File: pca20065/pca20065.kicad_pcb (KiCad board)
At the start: 6 copper layers, 53 x 53 mm, 319 parts, among them J1 MM8130-2600, J2 MM8130-2600, J3 HDR-3, 1mm, J4 SF72S006VBxR2500, J6 USB-C 2.0, M1 nRF9151-LACAA1A, P1 HDR-4, 1mm, P8 Pin Header 2x5, P9 Card Edge, 0.8mm, Q1 RV2C010UNT2L, Q13 DMC2990UDJ, Q14 RV2C010UNT2L, Q2 DMN2990UDJ, Q3 RV2C010UNT2L, Q4 DMN2990UDJ, Q5 RV2C010UNT2L, Q6 DMC2990UDJ, SW1 Switch, SW2 AYZ0102AGRLC, SW3 PB SW, SW4 L-KLS7-TS5401A-1.35-250-T, U1 NLAS5223BMNR2G, U10 TCK106AG, U11 nPM1300-QEAAC0, U12 FSA2466UMX, U13 TCK106AG, U14 TCK106AG, U15 MFFx_M2M_UICC, U16 NX3DV2567, U17 QM13345, U18 BMI270, U2 TCK106AG, U20 ADXL367, U21 nRF7002-QFAAB0, U22 BGS12xN6, U23 BME688, U24 TXS0102YZPR, U25 nPM6001-CAAAF0, U26 BMM350, U3 TCK106AG, U4 TCK106AG, U5 TCK108AG, U6 nRF5340-CMAAD0, U7 GD25LE255ELIG, U8 ECMF02-4CMX8, U9 SKY65943-11, X1 32MHz, X2 32.768kHz, X3 40MHz

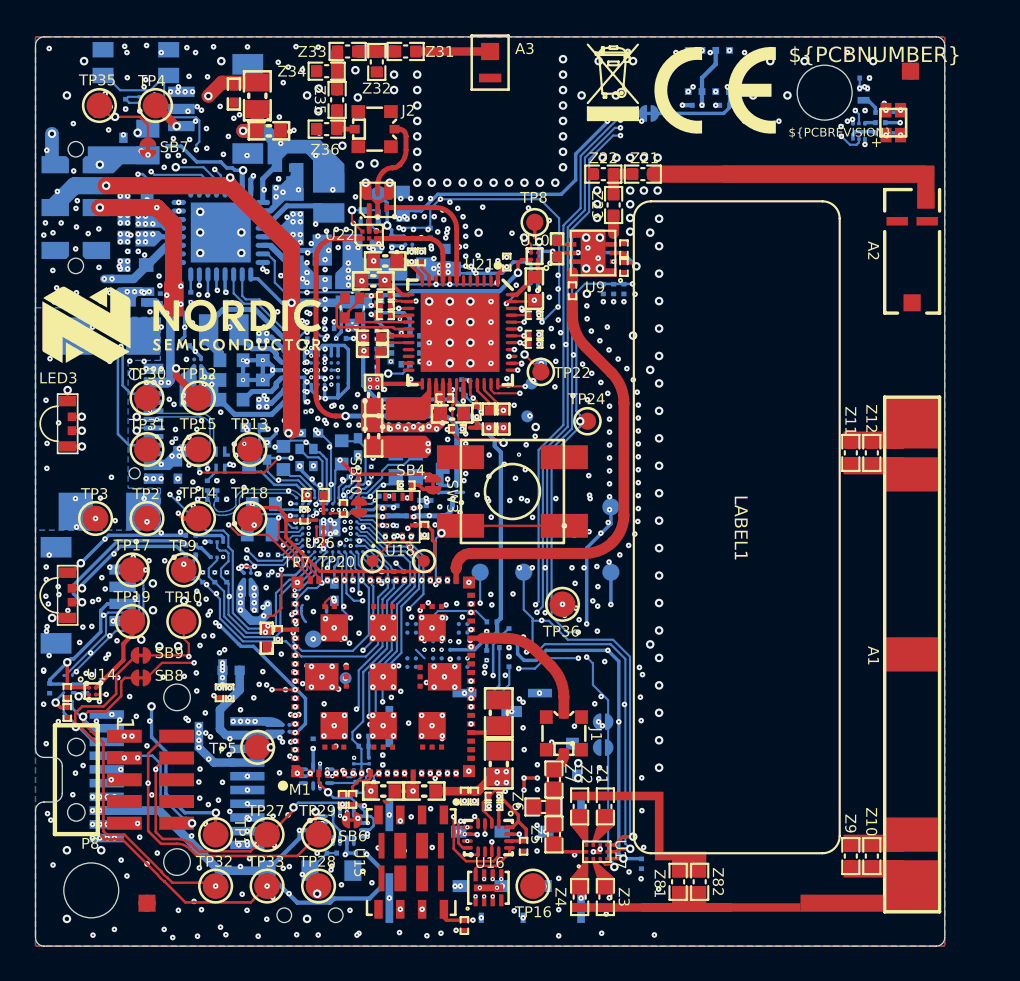
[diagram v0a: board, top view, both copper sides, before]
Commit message: Replaced nrf5340 with nrf54l15
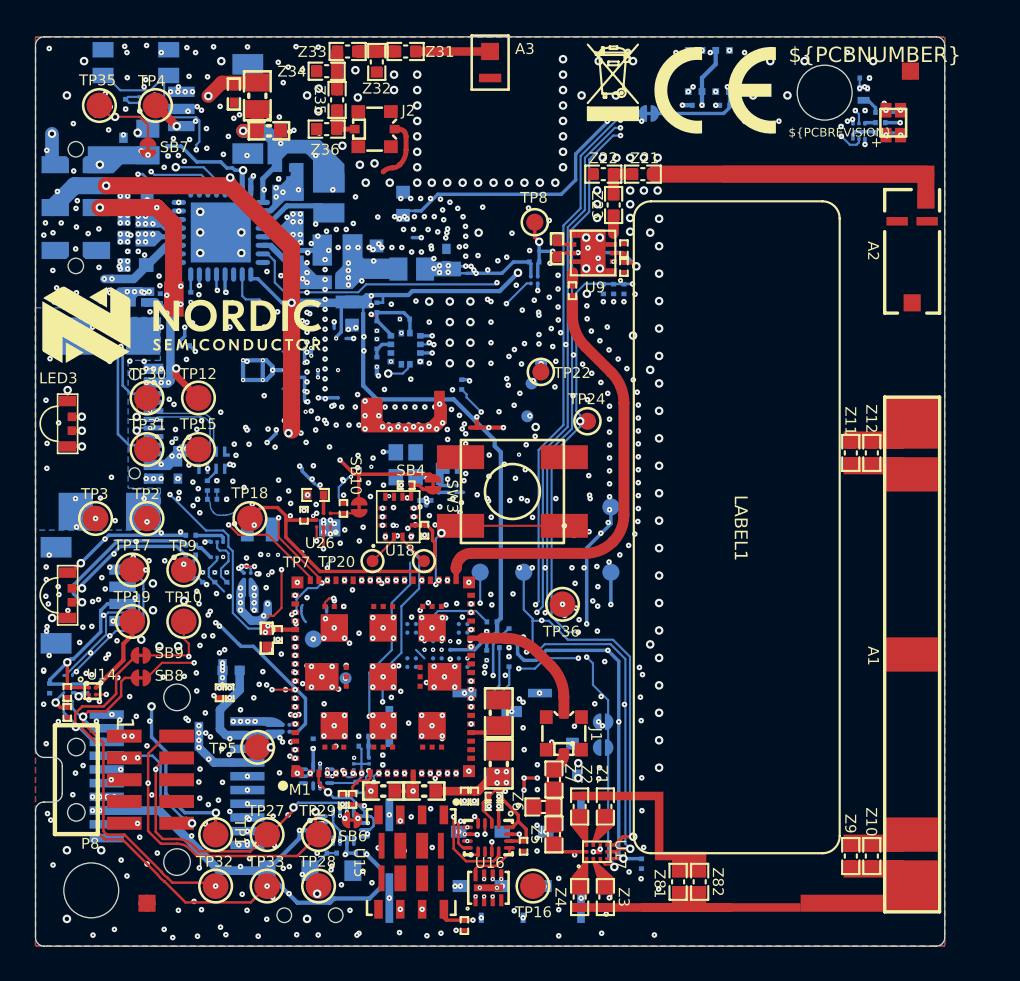
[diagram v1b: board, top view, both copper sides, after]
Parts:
- removed C12, C13, C19, C20, C21, C28, C41, C62: 100nF, pca20065-import-fps:CAPC0603X03L_C
- removed C15, C16, C17, C22, C23, C29, C45, C72, C73: 1.0µF, pca20065-import-fps:CAPC1005X04L
- removed C18: 2.2nF, pca20065-import-fps:CAPC0603X03L_C
- removed C24: 0.7pF, pca20065-import-fps:CAPC0603X03L_C
- removed C25: N.C., pca20065-import-fps:CAPC0603X03L_C_NC
- removed C26, C27, C63, C64, C65, C68, C81: 4.7µF, pca20065-import-fps:CAPC1608X06L
- removed C30, C67: 2.2µF, pca20065-import-fps:CAPC1608X06L
- removed C42: 2.2µF, pca20065-import-fps:CAPC1005X04L
- removed C60, C61: 0.47µF, pca20065-import-fps:CAPC0603X03L_C
- removed C66: 10nF, pca20065-import-fps:CAPC0603X03L_C
- removed C69: 22nF, pca20065-import-fps:CAPC0603X03L_C
- removed C70: 0.22µF, pca20065-import-fps:CAPC0603X03L_C
- removed C71: 2.2µF, pca20065-import-fps:CAPC0603X03L_C
- removed C77, C78, C80: 10µF, pca20065-import-fps:CAPC1608X06L
- removed C82, C83, C84, C85: 1.0µF, pca20065-import-fps:CAPC0603X03L_C
- removed F2: LFD_Diplexer, pca20065-import-fps:CAF-50P160X80-6N
- removed L1, L2: 10µH, pca20065-import-fps:INDC1608X06L
- removed L10: 470nH, pca20065-import-fps:INDC1608X06L
- removed L3, L4: 2.2nH, pca20065-import-fps:INDC0603X03L_C
- removed L6: 3.3µH, pca20065-import-fps:INDC2520X10N
- removed L9: 2.2µH, pca20065-import-fps:INDC2016X10N
- removed Q5: RV2C010UNT2L, pca20065-import-fps:DFN65P100X40-3L
- removed R10: 2R2, pca20065-import-fps:RESC1005X04L
- removed R11: 0R, pca20065-import-fps:RESC0603X03L_C
- removed R16, R4, R6: 150R, pca20065-import-fps:RESC0603X03L_C
- removed R25: N.C., pca20065-import-fps:RESC0603X03L_C_NC
- removed R33, R9: 1M0, pca20065-import-fps:RESC0603X03L_C
- removed R58, R59, R60, R61, R62: 100k, pca20065-import-fps:RESC0603X03L_C
- removed TP11: Ø1.0mm,SMD, pca20065-import-fps:TP_SMD_D1.0mm
- removed TP13, TP14: Ø1.5mm,SMD, pca20065-import-fps:TP_SMD_D1.5mm
- removed U10, U2: TCK106AG, pca20065-import-fps:BGA4C40P2X2_76X76X62
- removed U21: nRF7002-QFAAB0, pca20065-import-fps:QFN40P600X600X60-48N
- removed U22: BGS12xN6, pca20065-import-fps:TSNP-6-8
- removed U25: nPM6001-CAAAF0, pca20065-import-fps:BGA45C40P5X9_217X364X49
- removed U5: TCK108AG, pca20065-import-fps:BGA4C40P2X2_76X76X62
- removed U6: nRF5340-CMAAD0, pca20065-import-fps:BGA95C35P12X11_439X399X49
- removed X3: 40MHz, pca20065-import-fps:BT-XTAL_1612
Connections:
- net /Interface/nRF53_SWD.RST renamed /Interface/nRF54_SWD.RST
- net /nRF5340/BMI270_CS renamed /nRF54L15/BMI270_CS
- net /nRF5340/LTE_BLE_COEX renamed /nRF54L15/LTE_BLE_COEX
- net VDD_nRF53 renamed VDD_nRF54
- M1 pad 45: /nRF5340/WIFI_HOST_IF.VDDIO_CTRL -> (no net)
- M1 pad 47: /nRF5340/WIFI_HOST_IF.ENABLE -> (no net)
- M1 pad 56: /nRF5340/VCOM0.TXD -> /nRF54L15/VCOM0.TXD
- M1 pad 57: /nRF5340/VCOM0.RXD -> /nRF54L15/VCOM0.RXD
- M1 pad 61: /nRF5340/VCOM1.TXD -> /nRF54L15/VCOM1.TXD
- M1 pad 62: /nRF5340/VCOM1.RXD -> /nRF54L15/VCOM1.RXD
- M1 pad 77: /nRF5340/WIFI_HOST_IF.IRQ -> (no net)
- M1 pad 78: /nRF5340/WIFI_HOST_IF.SS -> (no net)
- P9 pad 1: VOUT_BUCK3 -> (no net)
- P9 pad 2: VBAT_nRF70 -> (no net)
- U11 pad 11: /Power_Supply/nPM60_READY -> (no net)
- U11 pad 29: /Power_Supply/nPM60_ENABLE -> (no net)
- U11 pad 8: /Power_Supply/RFFE_BLE_WIFI_ENABLE -> (no net)
- X1 pad 1: /nRF5340/XC1 -> /nRF54L15/XC1
- X1 pad 3: /nRF5340/XC2 -> /nRF54L15/XC2
- X2 pad 1: /nRF5340/XL1 -> /nRF54L15/XL1
- X2 pad 2: /nRF5340/XL2 -> /nRF54L15/XL2
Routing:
- net VBAT_nRF70: track 63.7 -> 0.00 mm, vias 34 -> 0
- net /RF_Frontend/2.4G_SW_CTRL: track 56.5 -> 0.00 mm, vias 9 -> 0
- net /nRF5340/WIFI_HOST_IF.IRQ: track 54.0 -> 0.00 mm, vias 10 -> 0
- net /nRF5340/WIFI_HOST_IF.VDDIO_CTRL: track 45.0 -> 0.00 mm, vias 6 -> 0
- net /nRF5340/WIFI_HOST_IF.SS: track 44.7 -> 0.00 mm, vias 10 -> 0
- net /Power_Supply/RFFE_BLE_WIFI_ENABLE: track 42.2 -> 0.00 mm, vias 6 -> 0
- net VOUT_BUCK3: track 36.9 -> 0.00 mm, vias 18 -> 0
- net /nRF5340/WIFI_HOST_IF.ENABLE: track 34.6 -> 0.00 mm, vias 6 -> 0
- net /nRF54L15/LTE_BLE_COEX: track 46.9 -> 13.1 mm, vias 14 -> 4
- net /nRF5340/COEX_WIFI.GRANT: track 30.0 -> 0.00 mm, vias 6 -> 0
- net VDD_nRF54: track 75.0 -> 45.5 mm, vias 40 -> 27
- net /nRF5340/COEX_WIFI.REQ: track 27.3 -> 0.00 mm, vias 4 -> 0
- net /Interface/TRACE.TRACE1: track 39.4 -> 14.5 mm, vias 8 -> 5
- net /RF_Frontend/BLE_RF: track 23.8 -> 0.00 mm, vias 1 -> 0
- net /nRF5340/COEX_WIFI.STATUS: track 22.2 -> 0.00 mm, vias 4 -> 0
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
